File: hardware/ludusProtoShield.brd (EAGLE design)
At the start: 59.7 x 53.3 mm, 65 parts, among them U1 ARDUINO, U2 TB6612FNG

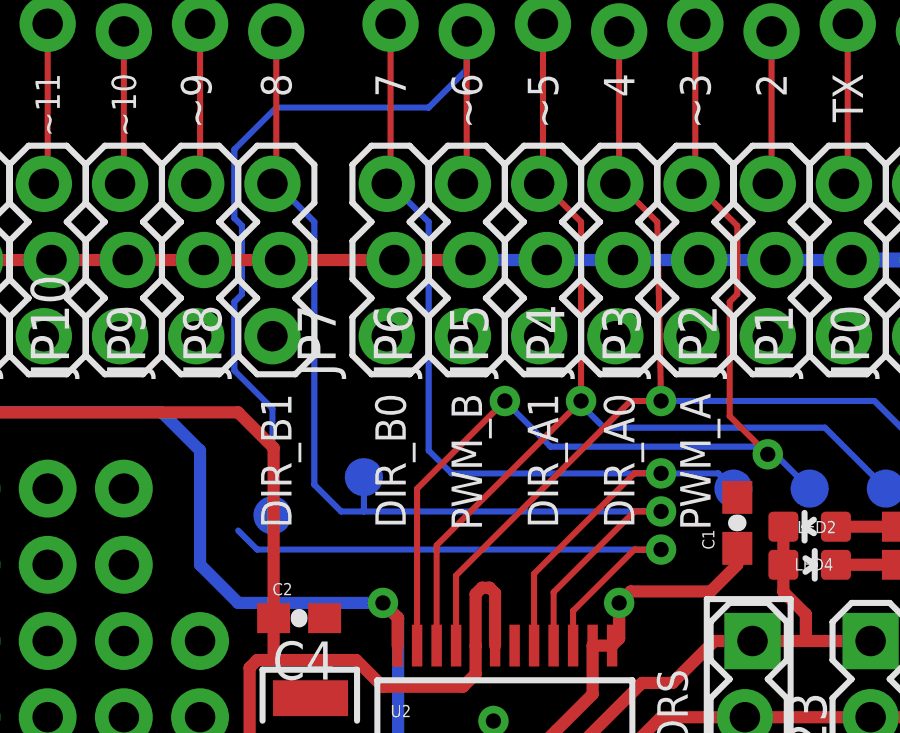
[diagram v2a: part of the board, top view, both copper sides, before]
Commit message: Revert "Revert "Updates to reflect changes for Issue #17 & #18""
This reverts commit 5692900b07c6701b416bef0e24551a599566d7ad.
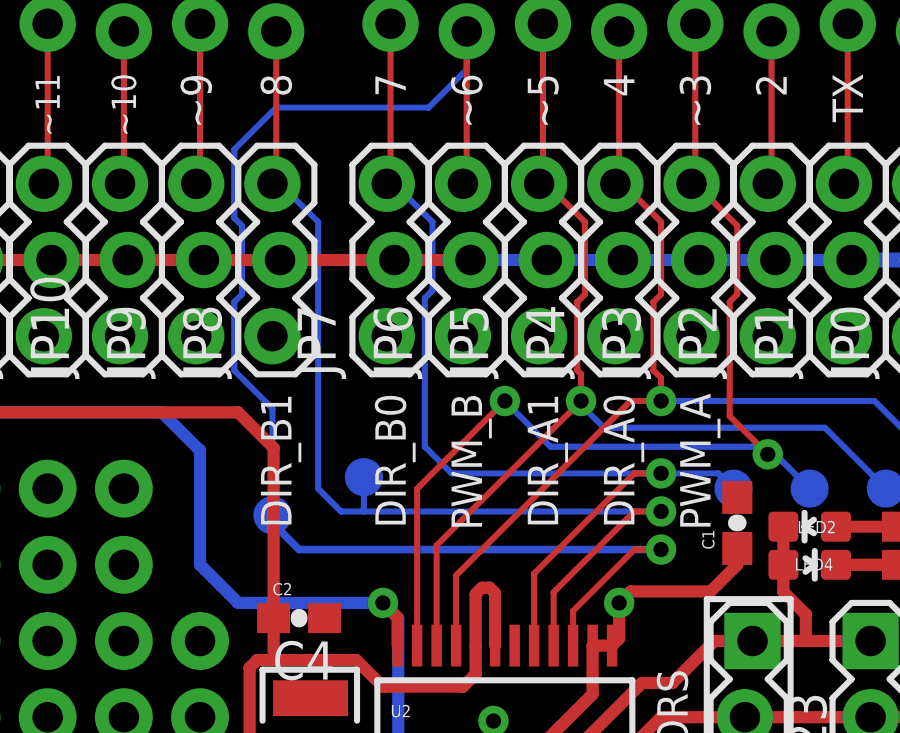
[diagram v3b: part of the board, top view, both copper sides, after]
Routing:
- net PWMB: track 48.6 -> 46.7 mm
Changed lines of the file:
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@@
 <wire x1="42.915" y1="31.485" x2="44.958" y2="33.528" width="0.2032" layer="1"/>
 <wire x1="45.847" y1="33.528" x2="44.958" y2="33.528" width="0.2032" layer="1"/>
-<wire x1="32.385" y1="33.528" x2="31.75" y2="34.163" width="0.2032" layer="16"/>
-<wire x1="32.385" y1="33.528" x2="32.893" y2="33.528" width="0.2032" layer="16"/>
-<wire x1="32.893" y1="33.528" x2="45.847" y2="33.528" width="0.2032" layer="16"/>
 <contactref element="TP6" pad="P$1"/>
-<wire x1="32.893" y1="34.671" x2="32.893" y2="33.528" width="0.2032" layer="16"/>
 <contactref element="U1" pad="D6"/>
 <contactref element="JP6" pad="3"/>
@@
 <wire x1="38.1" y1="48.26" x2="39.37" y2="49.53" width="0.2032" layer="16"/>
 <wire x1="39.37" y1="49.53" x2="39.37" y2="50.8" width="0.2032" layer="16"/>
+<wire x1="45.847" y1="33.528" x2="33.782" y2="33.528" width="0.254" layer="16"/>
+<wire x1="33.782" y1="33.528" x2="33.02" y2="34.29" width="0.254" layer="16"/>
+<wire x1="33.02" y1="34.29" x2="33.02" y2="34.544" width="0.254" layer="16"/>
+<wire x1="33.02" y1="34.544" x2="32.893" y2="34.671" width="0.254" layer="16"/>
 </signal>
 <signal name="VIN">
@@
 <wire x1="41.615" y1="32.725" x2="44.958" y2="36.068" width="0.2032" layer="1"/>
 <wire x1="45.847" y1="36.068" x2="38.862" y2="36.068" width="0.2032" layer="16"/>
-<wire x1="38.862" y1="36.068" x2="38.1" y2="36.83" width="0.2032" layer="16"/>
-<wire x1="38.1" y1="36.83" x2="38.1" y2="44.45" width="0.2032" layer="16"/>
+<wire x1="37.973" y1="36.957" x2="37.973" y2="41.91" width="0.2032" layer="16"/>
+<wire x1="37.973" y1="41.91" x2="38.227" y2="42.164" width="0.2032" layer="16"/>
+<wire x1="38.227" y1="42.164" x2="38.227" y2="44.45" width="0.2032" layer="16"/>
 <wire x1="36.83" y1="51.054" x2="36.83" y2="45.847" width="0.2032" layer="1"/>
 <wire x1="36.83" y1="45.847" x2="36.703" y2="45.72" width="0.2032" layer="1"/>
-<wire x1="36.703" y1="45.72" x2="36.83" y2="45.72" width="0.2032" layer="16"/>
-<wire x1="36.83" y1="45.72" x2="38.1" y2="44.45" width="0.2032" layer="16"/>
 <wire x1="45.847" y1="36.068" x2="44.958" y2="36.068" width="0.2032" layer="1"/>
 <contactref element="TP4" pad="P$1"/>
 <wire x1="45.847" y1="36.068" x2="47.752" y2="36.068" width="0.2032" layer="16"/>
 <wire x1="47.752" y1="36.068" x2="48.26" y2="35.56" width="0.2032" layer="16"/>
+<wire x1="37.973" y1="36.957" x2="38.862" y2="36.068" width="0.2032" layer="16"/>
+<wire x1="36.703" y1="45.72" x2="36.957" y2="45.72" width="0.2032" layer="16"/>
+<wire x1="36.957" y1="45.72" x2="38.227" y2="44.45" width="0.2032" layer="16"/>
 </signal>
 <signal name="AIN2">
@@
 <contactref element="U1" pad="D5"/>
 <contactref element="JP5" pad="3"/>
-<wire x1="43.18" y1="44.45" x2="43.18" y2="38.481" width="0.2032" layer="1"/>
 <wire x1="41.91" y1="51.054" x2="41.91" y2="45.847" width="0.2032" layer="1"/>
 <wire x1="41.91" y1="45.847" x2="41.783" y2="45.72" width="0.2032" layer="1"/>
-<wire x1="41.783" y1="45.72" x2="41.91" y2="45.72" width="0.2032" layer="1"/>
-<wire x1="41.91" y1="45.72" x2="43.18" y2="44.45" width="0.2032" layer="1"/>
 <contactref element="TP2" pad="P$1"/>
 <via x="43.18" y="38.481" extent="1-16" drill="0.508"/>
@@
 <wire x1="43.18" y1="38.481" x2="43.18" y2="38.354" width="0.2032" layer="16"/>
 <wire x1="43.18" y1="38.354" x2="43.942" y2="37.592" width="0.2032" layer="16"/>
+<wire x1="43.053" y1="41.783" x2="43.053" y2="39.497" width="0.2032" layer="1"/>
+<wire x1="43.053" y1="39.497" x2="43.18" y2="39.37" width="0.2032" layer="1"/>
+<wire x1="43.18" y1="38.481" x2="43.18" y2="39.37" width="0.2032" layer="1"/>
+<wire x1="43.307" y1="44.45" x2="43.307" y2="42.037" width="0.2032" layer="1"/>
+<wire x1="43.307" y1="42.037" x2="43.053" y2="41.783" width="0.2032" layer="1"/>
+<wire x1="41.783" y1="45.72" x2="42.037" y2="45.72" width="0.2032" layer="1"/>
+<wire x1="42.037" y1="45.72" x2="43.307" y2="44.45" width="0.2032" layer="1"/>
 </signal>
 <signal name="AIN1">
@@
 <contactref element="U1" pad="D4"/>
 <contactref element="JP4" pad="3"/>
-<wire x1="45.847" y1="38.481" x2="45.72" y2="44.45" width="0.2032" layer="1"/>
 <wire x1="44.45" y1="50.8" x2="44.45" y2="45.847" width="0.2032" layer="1"/>
 <wire x1="44.45" y1="45.847" x2="44.323" y2="45.72" width="0.2032" layer="1"/>
 <wire x1="44.323" y1="45.72" x2="44.45" y2="45.72" width="0.2032" layer="1"/>
-<wire x1="44.45" y1="45.72" x2="45.72" y2="44.45" width="0.2032" layer="1"/>
 <contactref element="TP1" pad="P$1"/>
 <via x="45.847" y="38.481" extent="1-16" drill="0.508"/>
@@
 <wire x1="45.847" y1="38.481" x2="52.959" y2="38.481" width="0.2032" layer="16"/>
 <wire x1="52.959" y1="38.481" x2="55.88" y2="35.56" width="0.2032" layer="16"/>
+<wire x1="45.593" y1="41.783" x2="45.593" y2="39.497" width="0.2032" layer="1"/>
+<wire x1="45.847" y1="38.481" x2="45.847" y2="39.243" width="0.2032" layer="1"/>
+<wire x1="45.847" y1="39.243" x2="45.593" y2="39.497" width="0.2032" layer="1"/>
+<wire x1="44.45" y1="45.72" x2="44.577" y2="45.72" width="0.254" layer="1"/>
+<wire x1="44.577" y1="45.72" x2="45.847" y2="44.45" width="0.2032" layer="1"/>
+<wire x1="45.847" y1="44.45" x2="45.847" y2="42.037" width="0.2032" layer="1"/>
+<wire x1="45.847" y1="42.037" x2="45.593" y2="41.783" width="0.2032" layer="1"/>
 </signal>
 <signal name="D11">
@@
 <contactref element="U1" pad="D8"/>
 <via x="45.847" y="34.798" extent="1-16" drill="0.508"/>
-<wire x1="34.29" y1="35.687" x2="34.29" y2="44.45" width="0.2032" layer="16"/>
+<wire x1="34.417" y1="35.56" x2="34.417" y2="44.45" width="0.2032" layer="16"/>
 <wire x1="42.265" y1="30.326" x2="42.265" y2="32.105" width="0.2032" layer="1"/>
 <wire x1="42.265" y1="32.105" x2="44.958" y2="34.798" width="0.2032" layer="1"/>
 <wire x1="45.847" y1="34.798" x2="44.958" y2="34.798" width="0.2032" layer="1"/>
-<wire x1="35.179" y1="34.798" x2="34.29" y2="35.687" width="0.2032" layer="16"/>
 <wire x1="35.179" y1="34.798" x2="35.941" y2="34.798" width="0.2032" layer="16"/>
 <wire x1="35.941" y1="34.798" x2="45.847" y2="34.798" width="0.2032" layer="16"/>
 <wire x1="33.02" y1="50.8" x2="33.02" y2="45.847" width="0.2032" layer="1"/>
 <wire x1="33.02" y1="45.847" x2="32.893" y2="45.72" width="0.2032" layer="1"/>
-<wire x1="32.893" y1="45.72" x2="33.02" y2="45.72" width="0.2032" layer="16"/>
-<wire x1="33.02" y1="45.72" x2="34.29" y2="44.45" width="0.2032" layer="16"/>
 <contactref element="TP5" pad="P$1"/>
 <wire x1="35.941" y1="35.941" x2="35.941" y2="34.798" width="0.2032" layer="16"/>
+<wire x1="35.179" y1="34.798" x2="35.179" y2="34.8107" width="0.2032" layer="16"/>
+<wire x1="32.893" y1="45.72" x2="33.02" y2="45.72" width="0.2032" layer="16"/>
+<wire x1="33.02" y1="45.72" x2="33.0327" y2="45.72" width="0.2032" layer="16"/>
+<wire x1="34.417" y1="35.56" x2="35.179" y2="34.798" width="0.2032" layer="16"/>
+<wire x1="33.0327" y1="45.72" x2="33.147" y2="45.72" width="0.2032" layer="16"/>
+<wire x1="33.147" y1="45.72" x2="34.417" y2="44.45" width="0.2032" layer="16"/>
 </signal>
 <signal name="N$20">

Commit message: Revert "Updates to reflect changes for Issue #17 & #18"
This reverts commit 8485361f9dfebb0a91455fa50c213d3bada30c15.
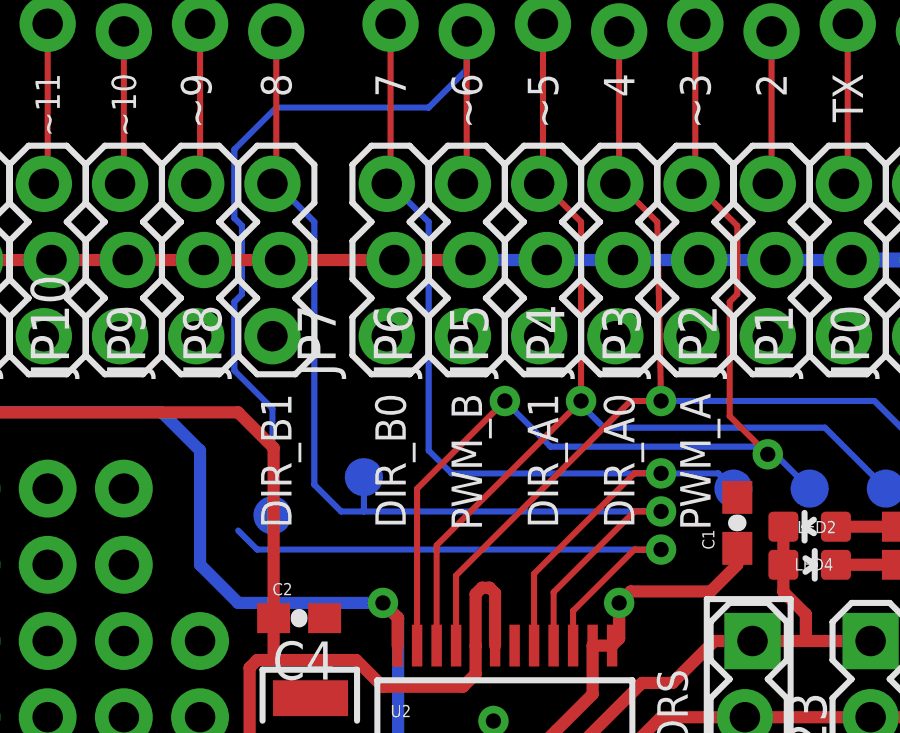
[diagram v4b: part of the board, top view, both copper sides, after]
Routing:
- net PWMB: track 46.7 -> 48.6 mm
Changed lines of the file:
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@@
 <wire x1="42.915" y1="31.485" x2="44.958" y2="33.528" width="0.2032" layer="1"/>
 <wire x1="45.847" y1="33.528" x2="44.958" y2="33.528" width="0.2032" layer="1"/>
+<wire x1="32.385" y1="33.528" x2="31.75" y2="34.163" width="0.2032" layer="16"/>
+<wire x1="32.385" y1="33.528" x2="32.893" y2="33.528" width="0.2032" layer="16"/>
+<wire x1="32.893" y1="33.528" x2="45.847" y2="33.528" width="0.2032" layer="16"/>
 <contactref element="TP6" pad="P$1"/>
+<wire x1="32.893" y1="34.671" x2="32.893" y2="33.528" width="0.2032" layer="16"/>
 <contactref element="U1" pad="D6"/>
 <contactref element="JP6" pad="3"/>
@@
 <wire x1="38.1" y1="48.26" x2="39.37" y2="49.53" width="0.2032" layer="16"/>
 <wire x1="39.37" y1="49.53" x2="39.37" y2="50.8" width="0.2032" layer="16"/>
-<wire x1="45.847" y1="33.528" x2="33.782" y2="33.528" width="0.254" layer="16"/>
-<wire x1="33.782" y1="33.528" x2="33.02" y2="34.29" width="0.254" layer="16"/>
-<wire x1="33.02" y1="34.29" x2="33.02" y2="34.544" width="0.254" layer="16"/>
-<wire x1="33.02" y1="34.544" x2="32.893" y2="34.671" width="0.254" layer="16"/>
 </signal>
 <signal name="VIN">
@@
 <wire x1="41.615" y1="32.725" x2="44.958" y2="36.068" width="0.2032" layer="1"/>
 <wire x1="45.847" y1="36.068" x2="38.862" y2="36.068" width="0.2032" layer="16"/>
-<wire x1="37.973" y1="36.957" x2="37.973" y2="41.91" width="0.2032" layer="16"/>
-<wire x1="37.973" y1="41.91" x2="38.227" y2="42.164" width="0.2032" layer="16"/>
-<wire x1="38.227" y1="42.164" x2="38.227" y2="44.45" width="0.2032" layer="16"/>
+<wire x1="38.862" y1="36.068" x2="38.1" y2="36.83" width="0.2032" layer="16"/>
+<wire x1="38.1" y1="36.83" x2="38.1" y2="44.45" width="0.2032" layer="16"/>
 <wire x1="36.83" y1="51.054" x2="36.83" y2="45.847" width="0.2032" layer="1"/>
 <wire x1="36.83" y1="45.847" x2="36.703" y2="45.72" width="0.2032" layer="1"/>
+<wire x1="36.703" y1="45.72" x2="36.83" y2="45.72" width="0.2032" layer="16"/>
+<wire x1="36.83" y1="45.72" x2="38.1" y2="44.45" width="0.2032" layer="16"/>
 <wire x1="45.847" y1="36.068" x2="44.958" y2="36.068" width="0.2032" layer="1"/>
 <contactref element="TP4" pad="P$1"/>
 <wire x1="45.847" y1="36.068" x2="47.752" y2="36.068" width="0.2032" layer="16"/>
 <wire x1="47.752" y1="36.068" x2="48.26" y2="35.56" width="0.2032" layer="16"/>
-<wire x1="37.973" y1="36.957" x2="38.862" y2="36.068" width="0.2032" layer="16"/>
-<wire x1="36.703" y1="45.72" x2="36.957" y2="45.72" width="0.2032" layer="16"/>
-<wire x1="36.957" y1="45.72" x2="38.227" y2="44.45" width="0.2032" layer="16"/>
 </signal>
 <signal name="AIN2">
@@
 <contactref element="U1" pad="D5"/>
 <contactref element="JP5" pad="3"/>
+<wire x1="43.18" y1="44.45" x2="43.18" y2="38.481" width="0.2032" layer="1"/>
 <wire x1="41.91" y1="51.054" x2="41.91" y2="45.847" width="0.2032" layer="1"/>
 <wire x1="41.91" y1="45.847" x2="41.783" y2="45.72" width="0.2032" layer="1"/>
+<wire x1="41.783" y1="45.72" x2="41.91" y2="45.72" width="0.2032" layer="1"/>
+<wire x1="41.91" y1="45.72" x2="43.18" y2="44.45" width="0.2032" layer="1"/>
 <contactref element="TP2" pad="P$1"/>
 <via x="43.18" y="38.481" extent="1-16" drill="0.508"/>
@@
 <wire x1="43.18" y1="38.481" x2="43.18" y2="38.354" width="0.2032" layer="16"/>
 <wire x1="43.18" y1="38.354" x2="43.942" y2="37.592" width="0.2032" layer="16"/>
-<wire x1="43.053" y1="41.783" x2="43.053" y2="39.497" width="0.2032" layer="1"/>
-<wire x1="43.053" y1="39.497" x2="43.18" y2="39.37" width="0.2032" layer="1"/>
-<wire x1="43.18" y1="38.481" x2="43.18" y2="39.37" width="0.2032" layer="1"/>
-<wire x1="43.307" y1="44.45" x2="43.307" y2="42.037" width="0.2032" layer="1"/>
-<wire x1="43.307" y1="42.037" x2="43.053" y2="41.783" width="0.2032" layer="1"/>
-<wire x1="41.783" y1="45.72" x2="42.037" y2="45.72" width="0.2032" layer="1"/>
-<wire x1="42.037" y1="45.72" x2="43.307" y2="44.45" width="0.2032" layer="1"/>
 </signal>
 <signal name="AIN1">
@@
 <contactref element="U1" pad="D4"/>
 <contactref element="JP4" pad="3"/>
+<wire x1="45.847" y1="38.481" x2="45.72" y2="44.45" width="0.2032" layer="1"/>
 <wire x1="44.45" y1="50.8" x2="44.45" y2="45.847" width="0.2032" layer="1"/>
 <wire x1="44.45" y1="45.847" x2="44.323" y2="45.72" width="0.2032" layer="1"/>
 <wire x1="44.323" y1="45.72" x2="44.45" y2="45.72" width="0.2032" layer="1"/>
+<wire x1="44.45" y1="45.72" x2="45.72" y2="44.45" width="0.2032" layer="1"/>
 <contactref element="TP1" pad="P$1"/>
 <via x="45.847" y="38.481" extent="1-16" drill="0.508"/>
@@
 <wire x1="45.847" y1="38.481" x2="52.959" y2="38.481" width="0.2032" layer="16"/>
 <wire x1="52.959" y1="38.481" x2="55.88" y2="35.56" width="0.2032" layer="16"/>
-<wire x1="45.593" y1="41.783" x2="45.593" y2="39.497" width="0.2032" layer="1"/>
-<wire x1="45.847" y1="38.481" x2="45.847" y2="39.243" width="0.2032" layer="1"/>
-<wire x1="45.847" y1="39.243" x2="45.593" y2="39.497" width="0.2032" layer="1"/>
-<wire x1="44.45" y1="45.72" x2="44.577" y2="45.72" width="0.254" layer="1"/>
-<wire x1="44.577" y1="45.72" x2="45.847" y2="44.45" width="0.2032" layer="1"/>
-<wire x1="45.847" y1="44.45" x2="45.847" y2="42.037" width="0.2032" layer="1"/>
-<wire x1="45.847" y1="42.037" x2="45.593" y2="41.783" width="0.2032" layer="1"/>
 </signal>
 <signal name="D11">
@@
 <contactref element="U1" pad="D8"/>
 <via x="45.847" y="34.798" extent="1-16" drill="0.508"/>
-<wire x1="34.417" y1="35.56" x2="34.417" y2="44.45" width="0.2032" layer="16"/>
+<wire x1="34.29" y1="35.687" x2="34.29" y2="44.45" width="0.2032" layer="16"/>
 <wire x1="42.265" y1="30.326" x2="42.265" y2="32.105" width="0.2032" layer="1"/>
 <wire x1="42.265" y1="32.105" x2="44.958" y2="34.798" width="0.2032" layer="1"/>
 <wire x1="45.847" y1="34.798" x2="44.958" y2="34.798" width="0.2032" layer="1"/>
+<wire x1="35.179" y1="34.798" x2="34.29" y2="35.687" width="0.2032" layer="16"/>
 <wire x1="35.179" y1="34.798" x2="35.941" y2="34.798" width="0.2032" layer="16"/>
 <wire x1="35.941" y1="34.798" x2="45.847" y2="34.798" width="0.2032" layer="16"/>
 <wire x1="33.02" y1="50.8" x2="33.02" y2="45.847" width="0.2032" layer="1"/>
 <wire x1="33.02" y1="45.847" x2="32.893" y2="45.72" width="0.2032" layer="1"/>
+<wire x1="32.893" y1="45.72" x2="33.02" y2="45.72" width="0.2032" layer="16"/>
+<wire x1="33.02" y1="45.72" x2="34.29" y2="44.45" width="0.2032" layer="16"/>
 <contactref element="TP5" pad="P$1"/>
 <wire x1="35.941" y1="35.941" x2="35.941" y2="34.798" width="0.2032" layer="16"/>
-<wire x1="35.179" y1="34.798" x2="35.179" y2="34.8107" width="0.2032" layer="16"/>
-<wire x1="32.893" y1="45.72" x2="33.02" y2="45.72" width="0.2032" layer="16"/>
-<wire x1="33.02" y1="45.72" x2="33.0327" y2="45.72" width="0.2032" layer="16"/>
-<wire x1="34.417" y1="35.56" x2="35.179" y2="34.798" width="0.2032" layer="16"/>
-<wire x1="33.0327" y1="45.72" x2="33.147" y2="45.72" width="0.2032" layer="16"/>
-<wire x1="33.147" y1="45.72" x2="34.417" y2="44.45" width="0.2032" layer="16"/>
 </signal>
 <signal name="N$20">
